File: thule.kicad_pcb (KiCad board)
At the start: 2 copper layers, 55.6 x 22.1 mm, 34 parts, among them J1 Conn_01x06, J2 USB_A, SW1 ~RST~, SW2 USR, U1 EFR32MG21x, U2 MIC5219-3.3YM5, U3 CP2102N-A01-GQFN24, Y1 32.768Khz, Y2 38.4Mhz

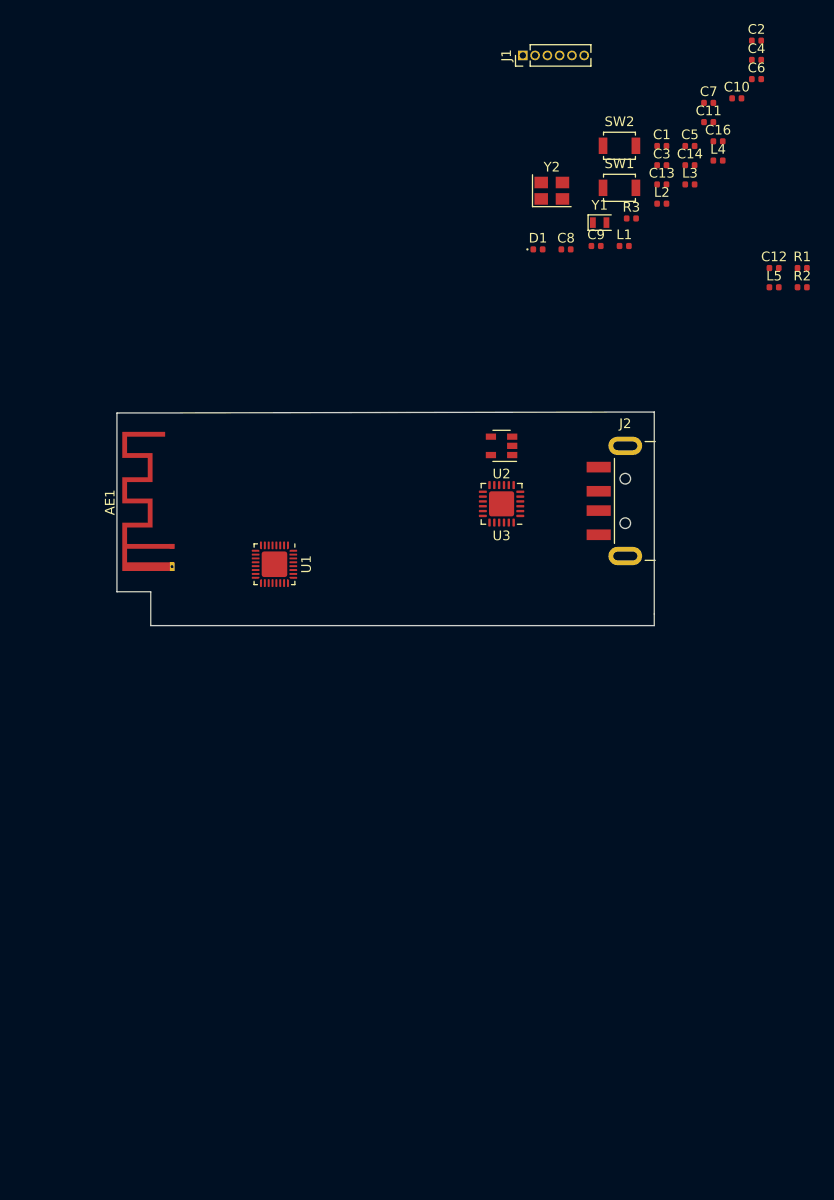
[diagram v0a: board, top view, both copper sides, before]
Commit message: Start routing, use bigger packages
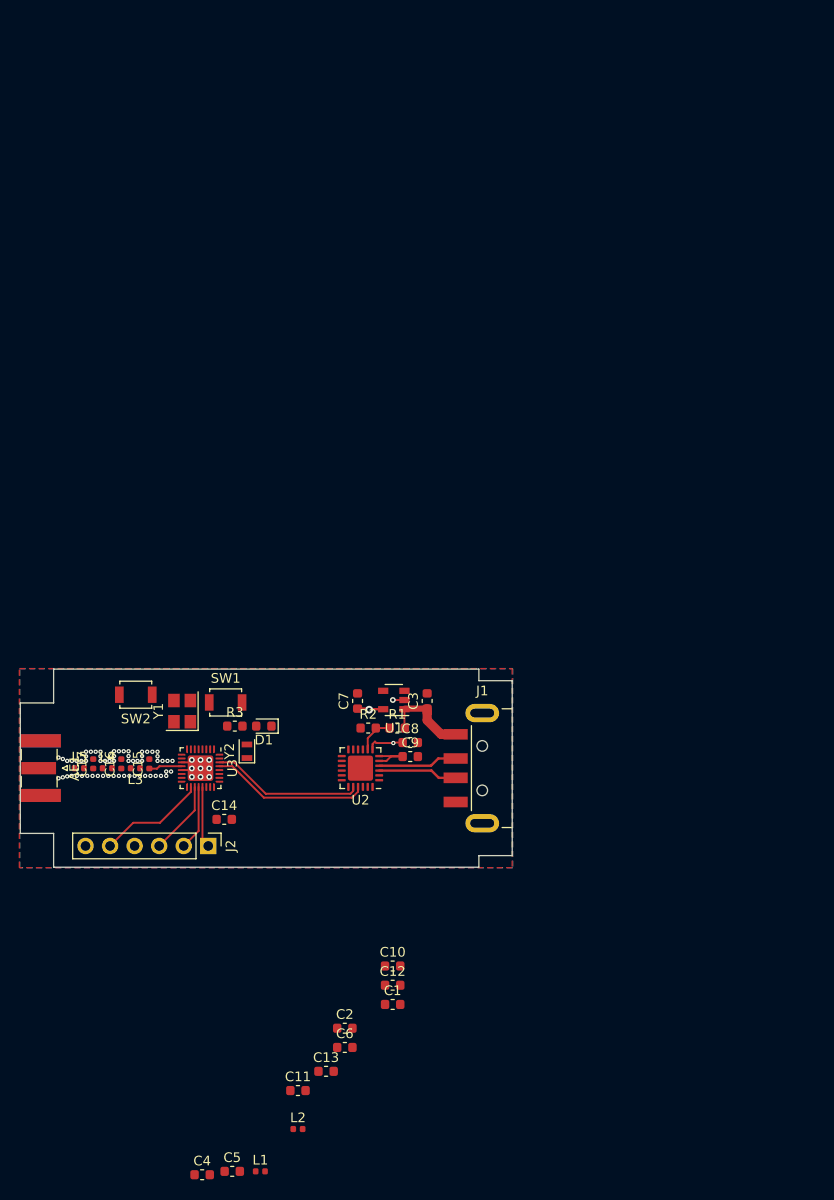
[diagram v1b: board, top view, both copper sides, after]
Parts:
- removed the J1 at (142.0, 83.0)
- removed the U1 at (116.3, 135.7)
- added C3: 10uF, Capacitor_SMD:C_0603_1608Metric, F.Cu at (132.1, 149.8)
- added C7: 10uF, Capacitor_SMD:C_0603_1608Metric, F.Cu at (124.9, 149.8)
- added J2: Conn_01x06, Connector_PinHeader_2.54mm:PinHeader_1x06_P2.54mm_Vertical, F.Cu at (109.5, 164.8)
- added U3: EFR32MG21x, Package_DFN_QFN:QFN-32-1EP_4x4mm_P0.4mm_EP2.65x2.65mm, F.Cu at (108.7, 156.8)
- AE1: footprint RF_Antenna:Texas_SWRA117D_2.4GHz_Right -> Connector_Coaxial:SMA_Samtec_SMA-J-P-X-ST-EM1_EdgeMount
- C1: renamed from C6; footprint Capacitor_SMD:C_0402_1005Metric -> Capacitor_SMD:C_0603_1608Metric
- C10: renamed from C2; footprint Capacitor_SMD:C_0402_1005Metric -> Capacitor_SMD:C_0603_1608Metric
- C11: renamed from C3; footprint Capacitor_SMD:C_0402_1005Metric -> Capacitor_SMD:C_0603_1608Metric
- C12: renamed from C4; footprint Capacitor_SMD:C_0402_1005Metric -> Capacitor_SMD:C_0603_1608Metric
- C13: renamed from C5; footprint Capacitor_SMD:C_0402_1005Metric -> Capacitor_SMD:C_0603_1608Metric
- C14: renamed from C1; footprint Capacitor_SMD:C_0402_1005Metric -> Capacitor_SMD:C_0603_1608Metric
- C2: renamed from C7; footprint Capacitor_SMD:C_0402_1005Metric -> Capacitor_SMD:C_0603_1608Metric
- C4: renamed from C8; footprint Capacitor_SMD:C_0402_1005Metric -> Capacitor_SMD:C_0603_1608Metric
- C5: renamed from C9; footprint Capacitor_SMD:C_0402_1005Metric -> Capacitor_SMD:C_0603_1608Metric
- C6: renamed from C11; footprint Capacitor_SMD:C_0402_1005Metric -> Capacitor_SMD:C_0603_1608Metric
- C8: renamed from C10; footprint Capacitor_SMD:C_0402_1005Metric -> Capacitor_SMD:C_0603_1608Metric
- C9: renamed from C16; value C_Small -> 0.1uF; footprint Capacitor_SMD:C_0402_1005Metric -> Capacitor_SMD:C_0603_1608Metric
- D1: footprint LED_SMD:LED_0402_1005Metric -> LED_SMD:LED_0603_1608Metric
- R1: renamed from R2; footprint Resistor_SMD:R_0402_1005Metric -> Resistor_SMD:R_0603_1608Metric
- R2: renamed from R1; footprint Resistor_SMD:R_0402_1005Metric -> Resistor_SMD:R_0603_1608Metric
- R3: footprint Resistor_SMD:R_0402_1005Metric -> Resistor_SMD:R_0603_1608Metric
- moved C12 102.9 mm to (128.5, 179.2)
- moved C10 102.9 mm to (128.5, 177.2)
- moved C11 102.9 mm to (118.7, 190.1)
- moved C4 102.9 mm to (108.8, 198.8)
- moved C5 102.9 mm to (111.9, 198.5)
- moved L1 102.9 mm to (114.8, 198.5)
- moved C1 102.9 mm to (128.5, 181.2)
- moved C13 102.9 mm to (121.6, 188.1)
- moved C2 102.9 mm to (123.6, 183.7)
- moved C6 102.9 mm to (123.6, 185.7)
- moved L2 102.9 mm to (118.7, 194.1)
- moved L5 91.2 mm to (96.1, 156.8)
- moved C17 87.1 mm to (97.5, 156.3), turned to 90 degrees
- moved C16 85.4 mm to (100.5, 156.3), turned to 90 degrees
- moved L4 85.1 mm to (99.0, 156.8)
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- renumbered C13 to C15, C14 to C16, C12 to C17, J2 to J1, L5 to L4, L4 to L5, SW2 to SW1, SW1 to SW2, U2 to U1, U3 to U2, Y2 to Y1, Y1 to Y2
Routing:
- net /NCP_UART_TX: track 0.00 -> 16.4 mm
- net /NCP_UART_RX: track 0.00 -> 15.7 mm
- net VDD: track 0.00 -> 11.6 mm, vias 0 -> 2
- net /SWCLK: track 0.00 -> 11.2 mm
- net VBUS: track 0.00 -> 9.10 mm
- net /D-: track 0.00 -> 8.22 mm
- net /D+: track 0.00 -> 8.22 mm
- net /SWDIO: track 0.00 -> 7.62 mm
- net /UART_RX: track 0.00 -> 6.74 mm
- net /UART_TX: track 0.00 -> 6.35 mm
- net GND: track 0.00 -> 5.43 mm, vias 0 -> 71
- net Net-(R1-Pad1): track 0.00 -> 3.98 mm
- net /ANT+: track 0.00 -> 3.46 mm
- added copper zone on B.Cu, net GND
- added copper zone on F.Cu, net GND
- added copper zone on In1.Cu, net GND
- added copper zone on In2.Cu, net VDD
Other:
- board size 55.6 x 22.1 mm -> 50.9 x 20.5 mm
- copper layers 2 -> 4
- rule via_min_drill: 0.3 -> 0.2
- rule via_min_size: 0.4 -> 0.45
